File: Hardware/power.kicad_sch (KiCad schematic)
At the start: 15 parts, among them J1 I2C ThroughHole, J3 I2C, J4 Interface, U7 AP7312-1833W6-7

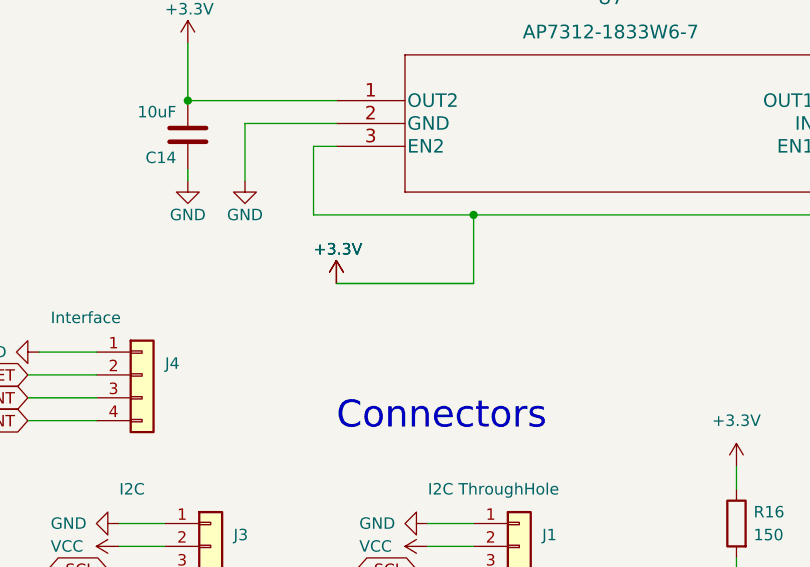
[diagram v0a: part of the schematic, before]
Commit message: Added pullup resistor to AS7341_INT line
Signed-off-by: lokimetasmith <lokimail@gmail.com>
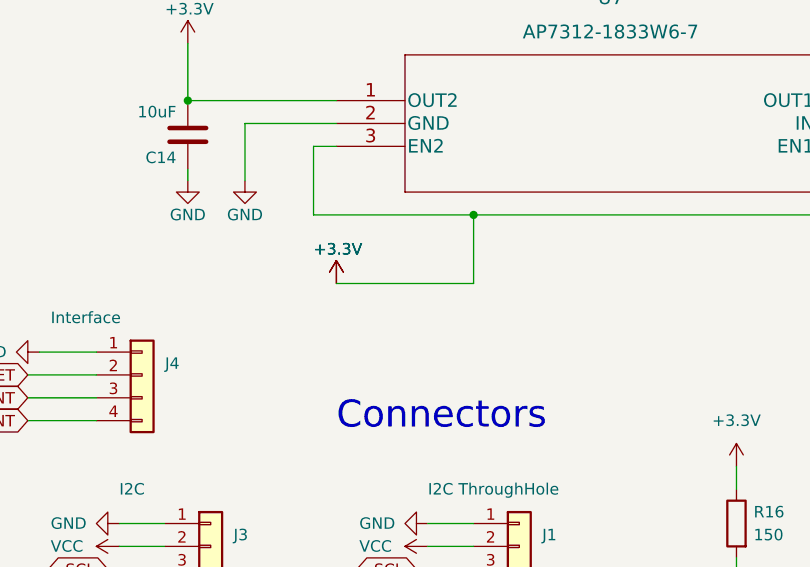
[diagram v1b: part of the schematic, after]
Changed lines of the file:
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@@
-    (stroke (width 0) (type default) (color 0 0 0 0))
-  )
-  (wire (pts (xy 176.53 110.49) (xy 191.77 110.49))
     (stroke (width 0) (type default) (color 0 0 0 0))
   )
@@
   (symbol (lib_id "power:+3.3V") (at 176.53 110.49 0) (unit 1)
     (in_bom yes) (on_board yes)
-    (property "Reference" "#PWR0132" (id 0) (at 176.53 114.3 0)
+    (property "Reference" "#PWR0134" (id 0) (at 176.53 114.3 0)
       (effects (font (size 1.27 1.27)) hide)
     )
